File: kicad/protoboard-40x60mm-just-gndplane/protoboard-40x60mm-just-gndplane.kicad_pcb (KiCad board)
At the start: 2 copper layers, 60 x 40 mm, 284 parts

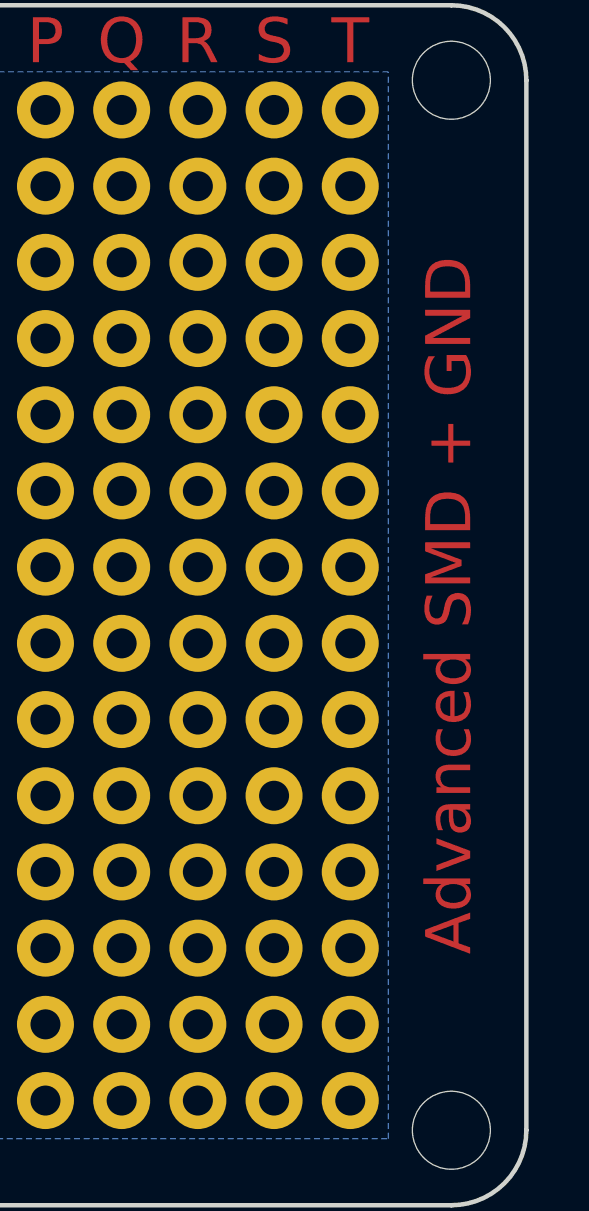
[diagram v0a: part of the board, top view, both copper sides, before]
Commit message: Update description for Gndplane Proto
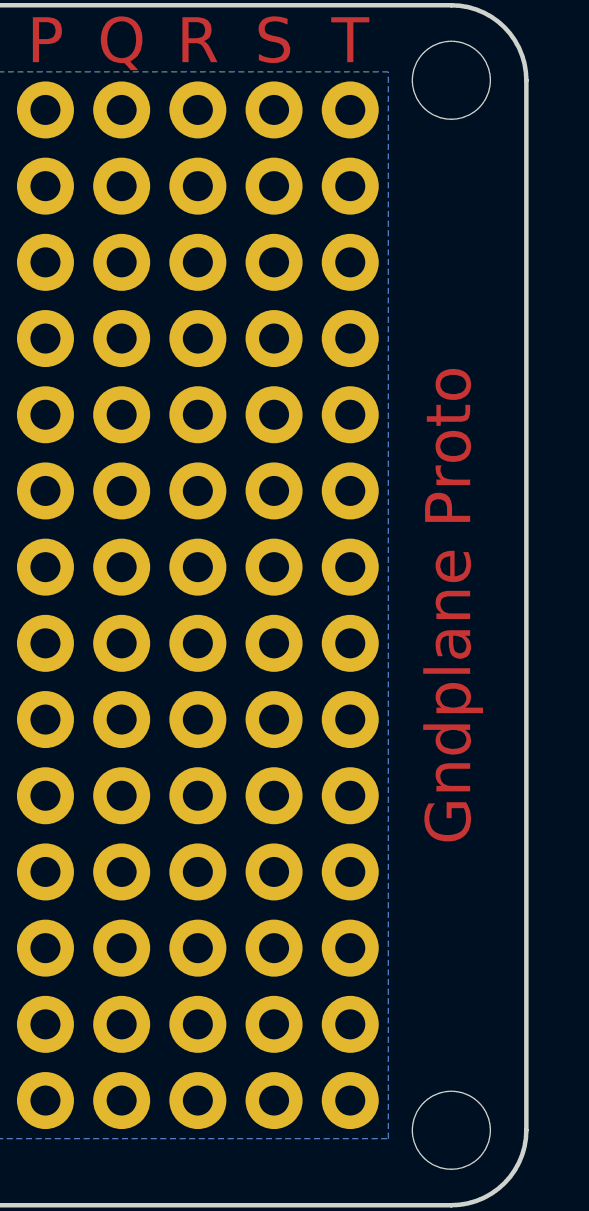
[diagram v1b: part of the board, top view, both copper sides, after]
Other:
- board text added: "Gndplane Proto"
- board text removed: "Advanced SMD + GND"
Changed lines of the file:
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@@
     (effects (font (size 1.5 1.5) (thickness 0.3)))
   )
-  (gr_text "Advanced SMD + GND" (at 173.432 99 90) (layer "F.Cu")
+  (gr_text "Gndplane Proto" (at 173.432 99 90) (layer "F.Cu")
     (effects (font (size 1.5 1.5) (thickness 0.3)))
   )
@@
     (effects (font (size 1.5 1.5) (thickness 0.3)) (justify mirror))
   )
-  (gr_text "Advanced SMD + GND" (at 173.432 99 -90) (layer "B.SilkS")
+  (gr_text "Gndplane Proto" (at 173.432 99 -90) (layer "B.SilkS")
     (effects (font (size 1.5 1.5) (thickness 0.3)) (justify mirror))
   )
@@
     (effects (font (size 1.5 1.5) (thickness 0.3)))
   )
-  (gr_text "Advanced SMD + GND" (at 173.432 99 90) (layer "F.Mask")
+  (gr_text "Gndplane Proto" (at 173.432 99 90) (layer "F.Mask")
     (effects (font (size 1.5 1.5) (thickness 0.3)))
   )
